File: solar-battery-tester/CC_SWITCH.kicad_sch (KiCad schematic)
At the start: 3 parts, among them Q9 Q_NMOS_GSD

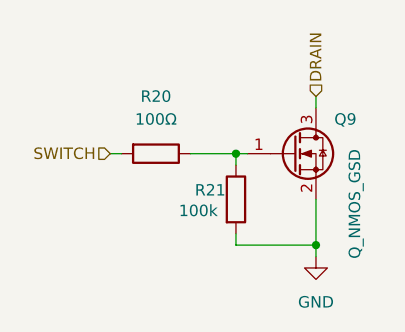
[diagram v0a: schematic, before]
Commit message: Fix reference conflicts and add JLCPCB part number
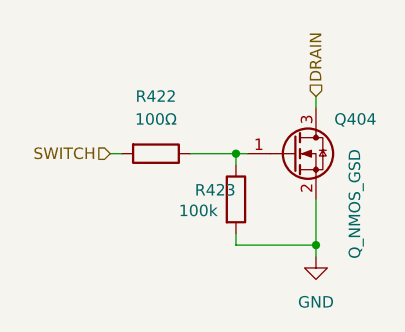
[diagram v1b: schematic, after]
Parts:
- renumbered Q9 to Q404, R20 to R422, R21 to R423
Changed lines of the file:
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@@
 		(dnp no)
 		(fields_autoplaced yes)
-		(property "Reference" "#PWR038"
+		(property "Reference" "#PWR0446"
 			(at 121.92 128.27 0)
 			(hide yes)
@@
 			(project "solar-battery-tester"
 				(path "/31e694ee-be1b-4b65-934d-7c826c4bd02c/2b3bc9df-be9d-4be6-be8c-06faa7fa7ccf"
-					(reference "#PWR039")
+					(reference "#PWR0447")
 					(unit 1)
 				)
 				(path "/31e694ee-be1b-4b65-934d-7c826c4bd02c/517a5ee3-30cf-4d8e-926a-65dedb85ce1d"
-					(reference "#PWR040")
+					(reference "#PWR0448")
 					(unit 1)
 				)
 				(path "/31e694ee-be1b-4b65-934d-7c826c4bd02c/5ac198e6-de12-4ad0-a59d-32655ca72e34"
-					(reference "#PWR043")
+					(reference "#PWR0451")
 					(unit 1)
 				)
 				(path "/31e694ee-be1b-4b65-934d-7c826c4bd02c/bceb424a-0e47-445d-8094-cecba2bf081f"
-					(reference "#PWR038")
+					(reference "#PWR0446")
 					(unit 1)
 				)
 				(path "/31e694ee-be1b-4b65-934d-7c826c4bd02c/f254e803-175b-4dc8-92e8-3385fc563738"
-					(reference "#PWR042")
+					(reference "#PWR0450")
 					(unit 1)
 				)
 				(path "/31e694ee-be1b-4b65-934d-7c826c4bd02c/fdf3b996-20b3-402f-8d68-d3aabb0e9006"
-					(reference "#PWR041")
+					(reference "#PWR0449")
 					(unit 1)
 				)
@@
 		(dnp no)
 		(fields_autoplaced yes)
-		(property "Reference" "R20"
+		(property "Reference" "R422"
 			(at 104.14 104.14 90)
 			(show_name no)
@@
 			(project "solar-battery-tester"
 				(path "/31e694ee-be1b-4b65-934d-7c826c4bd02c/2b3bc9df-be9d-4be6-be8c-06faa7fa7ccf"
-					(reference "R22")
+					(reference "R424")
 					(unit 1)
 				)
 				(path "/31e694ee-be1b-4b65-934d-7c826c4bd02c/517a5ee3-30cf-4d8e-926a-65dedb85ce1d"
-					(reference "R24")
+					(reference "R426")
 					(unit 1)
 				)
 				(path "/31e694ee-be1b-4b65-934d-7c826c4bd02c/5ac198e6-de12-4ad0-a59d-32655ca72e34"
-					(reference "R30")
+					(reference "R432")
 					(unit 1)
 				)
 				(path "/31e694ee-be1b-4b65-934d-7c826c4bd02c/bceb424a-0e47-445d-8094-cecba2bf081f"
-					(reference "R20")
+					(reference "R422")
 					(unit 1)
 				)
 				(path "/31e694ee-be1b-4b65-934d-7c826c4bd02c/f254e803-175b-4dc8-92e8-3385fc563738"
-					(reference "R28")
+					(reference "R430")
 					(unit 1)
 				)
 				(path "/31e694ee-be1b-4b65-934d-7c826c4bd02c/fdf3b996-20b3-402f-8d68-d3aabb0e9006"
-					(reference "R26")
+					(reference "R428")
 					(unit 1)
 				)
@@
 		(in_pos_files yes)
 		(dnp no)
-		(property "Reference" "Q9"
+		(property "Reference" "Q404"
 			(at 123.952 106.68 0)
 			(show_name no)
@@
 			(project "solar-battery-tester"
 				(path "/31e694ee-be1b-4b65-934d-7c826c4bd02c/2b3bc9df-be9d-4be6-be8c-06faa7fa7ccf"
-					(reference "Q11")
+					(reference "Q405")
 					(unit 1)
 				)
 				(path "/31e694ee-be1b-4b65-934d-7c826c4bd02c/517a5ee3-30cf-4d8e-926a-65dedb85ce1d"
-					(reference "Q12")
+					(reference "Q406")
 					(unit 1)
 				)
 				(path "/31e694ee-be1b-4b65-934d-7c826c4bd02c/5ac198e6-de12-4ad0-a59d-32655ca72e34"
-					(reference "Q15")
+					(reference "Q409")
 					(unit 1)
 				)
 				(path "/31e694ee-be1b-4b65-934d-7c826c4bd02c/bceb424a-0e47-445d-8094-cecba2bf081f"
-					(reference "Q9")
+					(reference "Q404")
 					(unit 1)
 				)
 				(path "/31e694ee-be1b-4b65-934d-7c826c4bd02c/f254e803-175b-4dc8-92e8-3385fc563738"
-					(reference "Q14")
+					(reference "Q408")
 					(unit 1)
 				)
 				(path "/31e694ee-be1b-4b65-934d-7c826c4bd02c/fdf3b996-20b3-402f-8d68-d3aabb0e9006"
-					(reference "Q13")
+					(reference "Q407")
 					(unit 1)
 				)
@@
 		(in_pos_files yes)
 		(dnp no)
-		(property "Reference" "R21"
+		(property "Reference" "R423"
 			(at 108.458 114.554 0)
 			(show_name no)
@@
 			(project "solar-battery-tester"
 				(path "/31e694ee-be1b-4b65-934d-7c826c4bd02c/2b3bc9df-be9d-4be6-be8c-06faa7fa7ccf"
-					(reference "R23")
+					(reference "R425")
 					(unit 1)
 				)
 				(path "/31e694ee-be1b-4b65-934d-7c826c4bd02c/517a5ee3-30cf-4d8e-926a-65dedb85ce1d"
-					(reference "R25")
+					(reference "R427")
 					(unit 1)
 				)
 				(path "/31e694ee-be1b-4b65-934d-7c826c4bd02c/5ac198e6-de12-4ad0-a59d-32655ca72e34"
-					(reference "R31")
+					(reference "R433")
 					(unit 1)
 				)
 				(path "/31e694ee-be1b-4b65-934d-7c826c4bd02c/bceb424a-0e47-445d-8094-cecba2bf081f"
-					(reference "R21")
+					(reference "R423")
 					(unit 1)
 				)
 				(path "/31e694ee-be1b-4b65-934d-7c826c4bd02c/f254e803-175b-4dc8-92e8-3385fc563738"
-					(reference "R29")
+					(reference "R431")
 					(unit 1)
 				)
 				(path "/31e694ee-be1b-4b65-934d-7c826c4bd02c/fdf3b996-20b3-402f-8d68-d3aabb0e9006"
-					(reference "R27")
-					(unit 1)
-				)
+					(reference "R429")
+					(unit 1)
+				)

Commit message: Fix DRC and ERC errors
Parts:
- renumbered Q404 to Q7, R422 to R25, R423 to R26
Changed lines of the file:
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@@
 		(dnp no)
 		(fields_autoplaced yes)
-		(property "Reference" "#PWR0446"
+		(property "Reference" "#PWR052"
 			(at 121.92 128.27 0)
 			(hide yes)
@@
 			(project "solar-battery-tester"
 				(path "/31e694ee-be1b-4b65-934d-7c826c4bd02c/2b3bc9df-be9d-4be6-be8c-06faa7fa7ccf"
-					(reference "#PWR0447")
+					(reference "#PWR053")
 					(unit 1)
 				)
 				(path "/31e694ee-be1b-4b65-934d-7c826c4bd02c/517a5ee3-30cf-4d8e-926a-65dedb85ce1d"
-					(reference "#PWR0448")
+					(reference "#PWR054")
 					(unit 1)
 				)
 				(path "/31e694ee-be1b-4b65-934d-7c826c4bd02c/5ac198e6-de12-4ad0-a59d-32655ca72e34"
-					(reference "#PWR0451")
+					(reference "#PWR057")
 					(unit 1)
 				)
 				(path "/31e694ee-be1b-4b65-934d-7c826c4bd02c/bceb424a-0e47-445d-8094-cecba2bf081f"
-					(reference "#PWR0446")
+					(reference "#PWR052")
 					(unit 1)
 				)
 				(path "/31e694ee-be1b-4b65-934d-7c826c4bd02c/f254e803-175b-4dc8-92e8-3385fc563738"
-					(reference "#PWR0450")
+					(reference "#PWR056")
 					(unit 1)
 				)
 				(path "/31e694ee-be1b-4b65-934d-7c826c4bd02c/fdf3b996-20b3-402f-8d68-d3aabb0e9006"
-					(reference "#PWR0449")
+					(reference "#PWR055")
 					(unit 1)
 				)
@@
 		(dnp no)
 		(fields_autoplaced yes)
-		(property "Reference" "R422"
+		(property "Reference" "R25"
 			(at 104.14 104.14 90)
 			(show_name no)
@@
 			(project "solar-battery-tester"
 				(path "/31e694ee-be1b-4b65-934d-7c826c4bd02c/2b3bc9df-be9d-4be6-be8c-06faa7fa7ccf"
-					(reference "R424")
+					(reference "R27")
 					(unit 1)
 				)
 				(path "/31e694ee-be1b-4b65-934d-7c826c4bd02c/517a5ee3-30cf-4d8e-926a-65dedb85ce1d"
-					(reference "R426")
+					(reference "R29")
 					(unit 1)
 				)
 				(path "/31e694ee-be1b-4b65-934d-7c826c4bd02c/5ac198e6-de12-4ad0-a59d-32655ca72e34"
-					(reference "R432")
+					(reference "R35")
 					(unit 1)
 				)
 				(path "/31e694ee-be1b-4b65-934d-7c826c4bd02c/bceb424a-0e47-445d-8094-cecba2bf081f"
-					(reference "R422")
+					(reference "R25")
 					(unit 1)
 				)
 				(path "/31e694ee-be1b-4b65-934d-7c826c4bd02c/f254e803-175b-4dc8-92e8-3385fc563738"
-					(reference "R430")
+					(reference "R33")
 					(unit 1)
 				)
 				(path "/31e694ee-be1b-4b65-934d-7c826c4bd02c/fdf3b996-20b3-402f-8d68-d3aabb0e9006"
-					(reference "R428")
+					(reference "R31")
 					(unit 1)
 				)
@@
 		(in_pos_files yes)
 		(dnp no)
-		(property "Reference" "Q404"
+		(property "Reference" "Q7"
 			(at 123.952 106.68 0)
 			(show_name no)
@@
 			(project "solar-battery-tester"
 				(path "/31e694ee-be1b-4b65-934d-7c826c4bd02c/2b3bc9df-be9d-4be6-be8c-06faa7fa7ccf"
-					(reference "Q405")
+					(reference "Q8")
 					(unit 1)
 				)
 				(path "/31e694ee-be1b-4b65-934d-7c826c4bd02c/517a5ee3-30cf-4d8e-926a-65dedb85ce1d"
-					(reference "Q406")
+					(reference "Q9")
 					(unit 1)
 				)
 				(path "/31e694ee-be1b-4b65-934d-7c826c4bd02c/5ac198e6-de12-4ad0-a59d-32655ca72e34"
-					(reference "Q409")
+					(reference "Q12")
 					(unit 1)
 				)
 				(path "/31e694ee-be1b-4b65-934d-7c826c4bd02c/bceb424a-0e47-445d-8094-cecba2bf081f"
-					(reference "Q404")
+					(reference "Q7")
 					(unit 1)
 				)
 				(path "/31e694ee-be1b-4b65-934d-7c826c4bd02c/f254e803-175b-4dc8-92e8-3385fc563738"
-					(reference "Q408")
+					(reference "Q11")
 					(unit 1)
 				)
 				(path "/31e694ee-be1b-4b65-934d-7c826c4bd02c/fdf3b996-20b3-402f-8d68-d3aabb0e9006"
-					(reference "Q407")
+					(reference "Q10")
 					(unit 1)
 				)
@@
 		(in_pos_files yes)
 		(dnp no)
-		(property "Reference" "R423"
+		(property "Reference" "R26"
 			(at 108.458 114.554 0)
 			(show_name no)
@@
 			(project "solar-battery-tester"
 				(path "/31e694ee-be1b-4b65-934d-7c826c4bd02c/2b3bc9df-be9d-4be6-be8c-06faa7fa7ccf"
-					(reference "R425")
+					(reference "R28")
 					(unit 1)
 				)
 				(path "/31e694ee-be1b-4b65-934d-7c826c4bd02c/517a5ee3-30cf-4d8e-926a-65dedb85ce1d"
-					(reference "R427")
+					(reference "R30")
 					(unit 1)
 				)
 				(path "/31e694ee-be1b-4b65-934d-7c826c4bd02c/5ac198e6-de12-4ad0-a59d-32655ca72e34"
-					(reference "R433")
+					(reference "R36")
 					(unit 1)
 				)
 				(path "/31e694ee-be1b-4b65-934d-7c826c4bd02c/bceb424a-0e47-445d-8094-cecba2bf081f"
-					(reference "R423")
+					(reference "R26")
 					(unit 1)
 				)
 				(path "/31e694ee-be1b-4b65-934d-7c826c4bd02c/f254e803-175b-4dc8-92e8-3385fc563738"
-					(reference "R431")
+					(reference "R34")
 					(unit 1)
 				)
 				(path "/31e694ee-be1b-4b65-934d-7c826c4bd02c/fdf3b996-20b3-402f-8d68-d3aabb0e9006"
-					(reference "R429")
-					(unit 1)
-				)
+					(reference "R32")
+					(unit 1)
+				)
